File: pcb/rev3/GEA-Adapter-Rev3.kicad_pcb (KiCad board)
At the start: 2 copper layers, 88.7 x 40 mm, 109 parts, among them J1 8P8C, J3 TC2030, J4 USB_C_Receptacle_USB2.0_16P, Q3 CJ3407, Q4 CJ3407, Q5 MMBT3904, SW1 SW_Push, SW2 SW_Push, U10 TPS22810DBVR, U2 ESP32-C3-WROOM-02, U4 74LVC2G07, U5 74LVC2G07_3v3, U6 AP2112K-3.3, U7 USBLC6-2SC6, U8 AP63205WU, U9 TPS22810DBVR

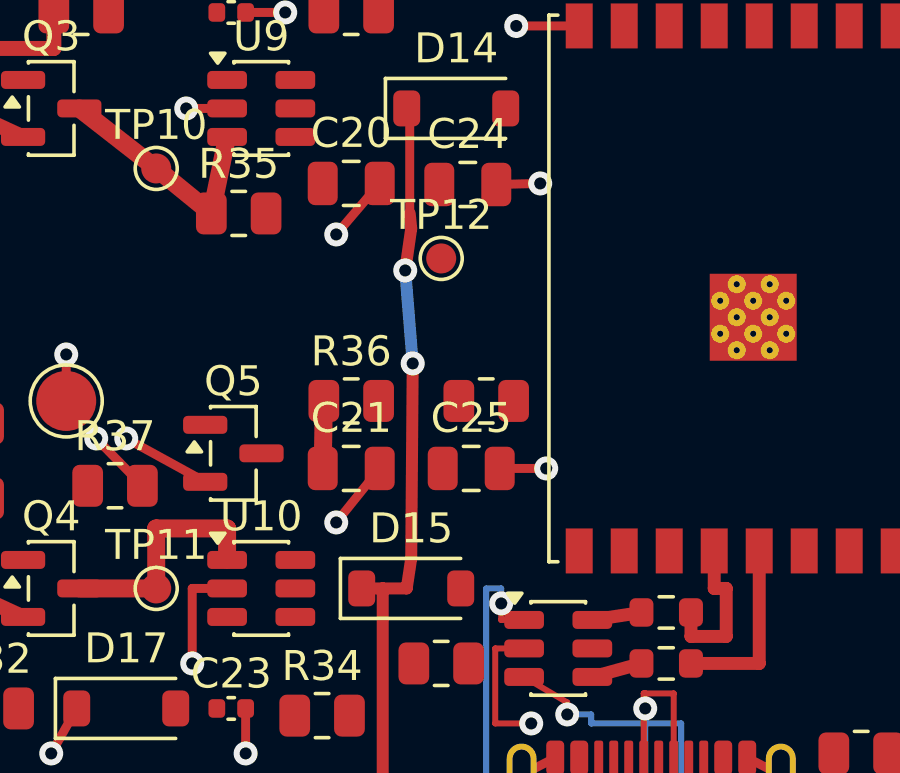
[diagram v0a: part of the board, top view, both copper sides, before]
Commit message: feat(pcb): route rev3a switch outputs
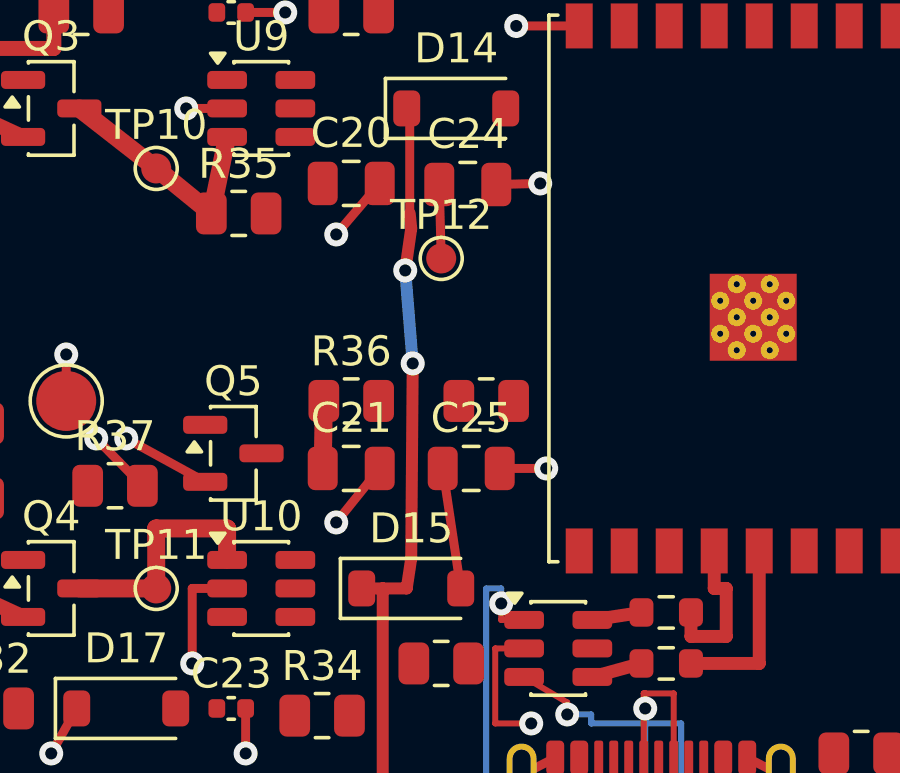
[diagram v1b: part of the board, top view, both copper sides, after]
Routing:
- net PIN3_SW_OUT: track 0.00 -> 4.04 mm
- net PIN1_SW_OUT: track 0.00 -> 2.47 mm
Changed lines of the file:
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@@
+	)
+	(segment
+		(start 65.05 23)
+		(end 65.65 27)
+		(width 0.3)
+		(layer "F.Cu")
+		(net 44)
 	)
 	(segment
@@
 	)
 	(segment
+		(start 64.935456 13.535277)
+		(end 65 16)
+		(width 0.3)
+		(layer "F.Cu")
+		(net 47)
+	)
+	(segment

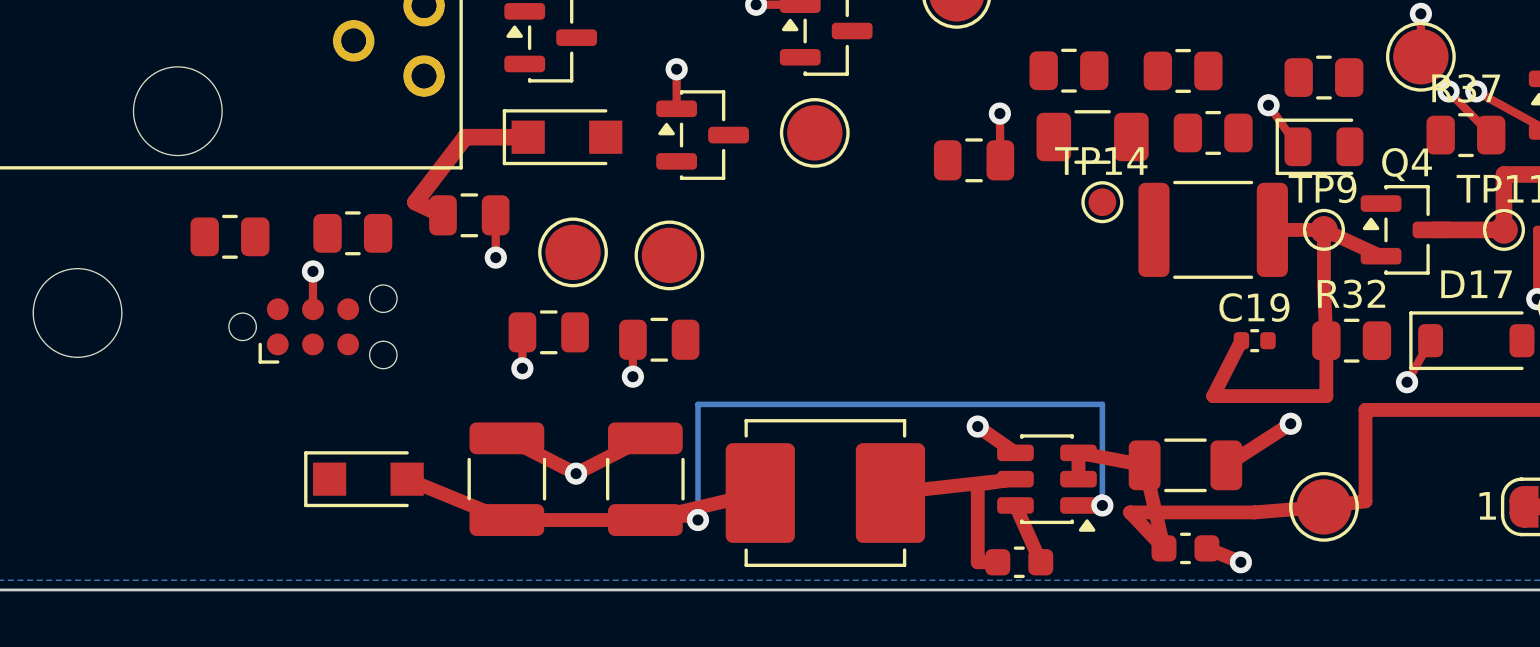
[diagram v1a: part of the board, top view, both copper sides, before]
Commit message: feat(pcb): reinforce rev3a buck output path
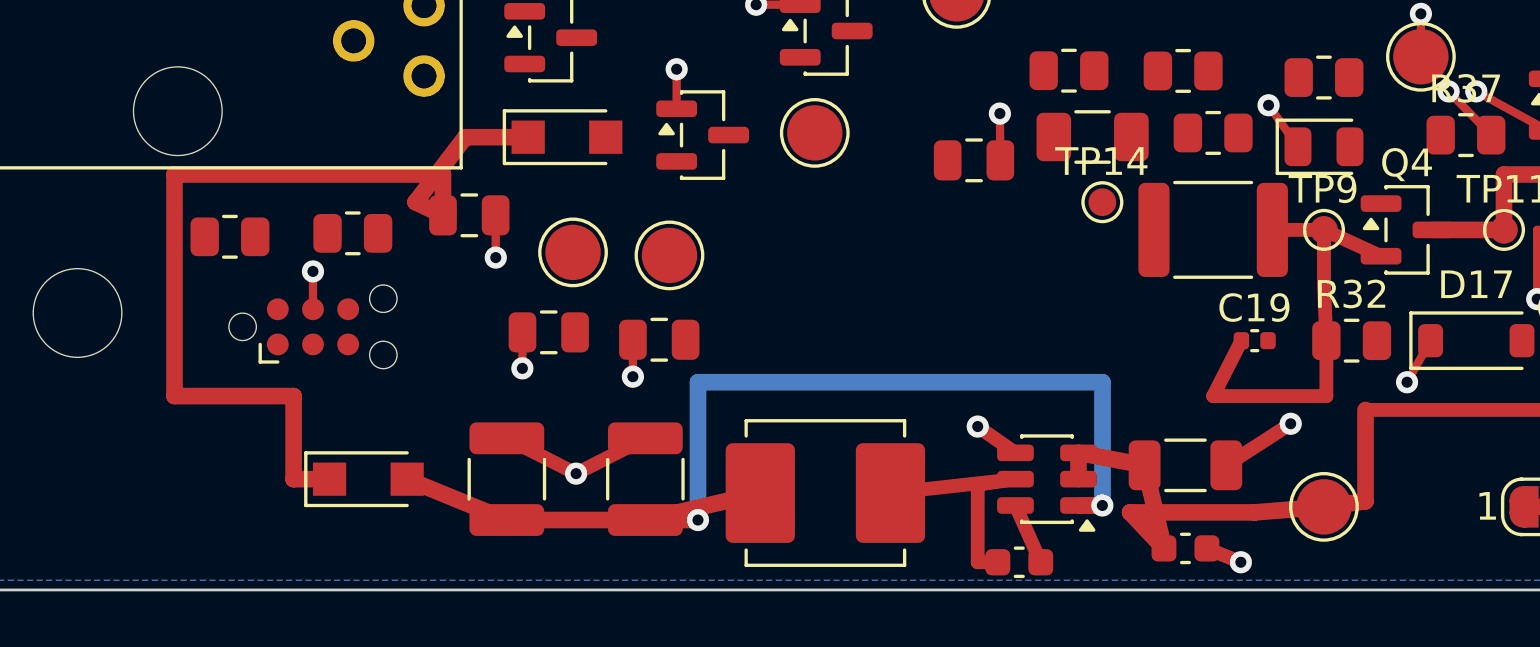
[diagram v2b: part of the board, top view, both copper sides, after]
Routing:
- net +5V: track 6.33 -> 34.1 mm
- net /BUCK_5V: track 38.3 -> 39.9 mm
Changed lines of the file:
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@@
+	)
+	(segment
+		(start 17.1947 25)
+		(end 17.1947 26.4745)
+		(width 0.6)
+		(layer "F.Cu")
+		(net 2)
 	)
 	(segment
@@
 	)
 	(segment
+		(start 7.5 33)
+		(end 7.5 25)
+		(width 0.6)
+		(layer "F.Cu")
+		(net 2)
+	)
+	(segment
+		(start 11.8 33)
+		(end 7.5 33)
+		(width 0.6)
+		(layer "F.Cu")
+		(net 2)
+	)
+	(segment
+		(start 13.1 36)
+		(end 11.8 36)
+		(width 0.6)
+		(layer "F.Cu")
+		(net 2)
+	)
+	(segment
+		(start 7.5 25)
+		(end 17.1947 25)
+		(width 0.6)
+		(layer "F.Cu")
+		(net 2)
+	)
+	(segment
 		(start 18 23.653262)
 		(end 16.2 26)
@@
 	)
 	(segment
+		(start 11.8 36)
+		(end 11.8 33)
+		(width 0.6)
+		(layer "F.Cu")
+		(net 2)
+	)
+	(segment
 		(start 16.2 26)
 		(end 17.194716 26.474524)
@@
 		(start 19.5 37.475)
 		(end 15.9 36)
-		(width 0.5)
+		(width 0.6)
 		(layer "F.Cu")
 		(net 5)
@@
 		(start 26.4 37.475)
 		(end 24.5 37.475)
-		(width 0.2)
+		(width 0.6)
 		(layer "F.Cu")
 		(net 5)
@@
 		(start 28.65 36.5)
 		(end 24.5 37.475)
-		(width 0.5)
+		(width 0.6)
 		(layer "F.Cu")
 		(net 5)
@@
 		(start 24.5 37.475)
 		(end 19.5 37.475)
-		(width 0.5)
+		(width 0.6)
 		(layer "F.Cu")
 		(net 5)
@@
 		(start 40.1375 36.95)
 		(end 41 36.95)
-		(width 0.2)
+		(width 0.6)
 		(layer "F.Cu")
 		(net 5)
@@
 	)
 	(segment
-		(start 41 33.299999)
-		(end 26.4 33.299999)
-		(width 0.2)
+		(start 41 32.5)
+		(end 26.4 32.5)
+		(width 0.6)
 		(layer "B.Cu")
 		(net 5)
 	)
 	(segment
-		(start 26.4 33.299999)
+		(start 26.4 32.5)
 		(end 26.4 37.475)
-		(width 0.2)
+		(width 0.6)
 		(layer "B.Cu")
 		(net 5)
@@
 	(segment
 		(start 41 36.95)
-		(end 41 33.299999)
-		(width 0.2)
+		(end 41 32.5)
+		(width 0.6)
 		(layer "B.Cu")
 		(net 5)
@@
 		(start 50.5 36.8)
 		(end 49 37)
-		(width 0.5)
+		(width 0.6)
 		(layer "F.Cu")
 		(net 61)
@@
 		(start 40.1375 36)
 		(end 40.1375 35.05)
-		(width 0.5)
+		(width 0.6)
 		(layer "F.Cu")
 		(net 61)
@@
 		(start 42.525 35.5)
 		(end 43.225 38.5)
-		(width 0.5)
+		(width 0.6)
 		(layer "F.Cu")
 		(net 61)
@@
 		(start 40.1375 35.05)
 		(end 42.525 35.5)
-		(width 0.5)
+		(width 0.6)
 		(layer "F.Cu")
 		(net 61)
@@
 		(start 42 37.2)
 		(end 46.5 37.2)
-		(width 0.5)
+		(width 0.6)
 		(layer "F.Cu")
 		(net 61)
@@
 		(start 46.5 37.2)
 		(end 49 37)
-		(width 0.5)
+		(width 0.6)
 		(layer "F.Cu")
 		(net 61)
@@
 		(start 43.225 38.5)
 		(end 42 37.2)
-		(width 0.5)
+		(width 0.6)
 		(layer "F.Cu")
 		(net 61)
@@
 		(start 50.5 33.5)
 		(end 50.5 36.8)
-		(width 0.5)
-		(layer "F.Cu")
-		(net 61)
+		(width 0.6)
+		(layer "F.Cu")
+		(net 61)

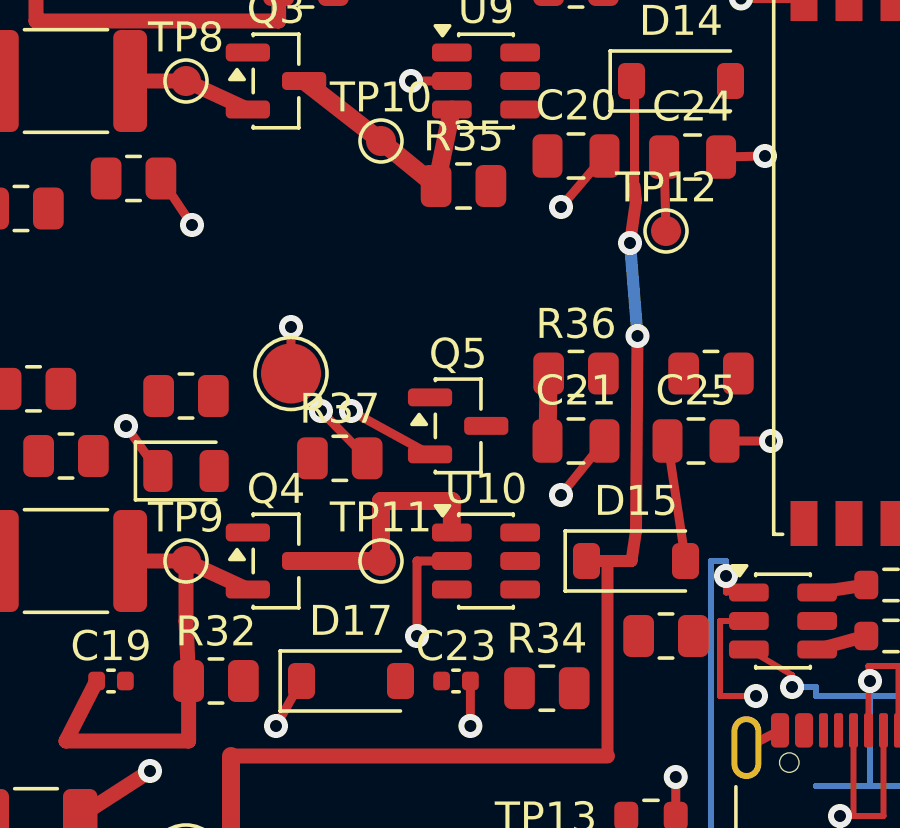
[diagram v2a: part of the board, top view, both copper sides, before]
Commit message: feat(pcb): route rev3a input priority controls
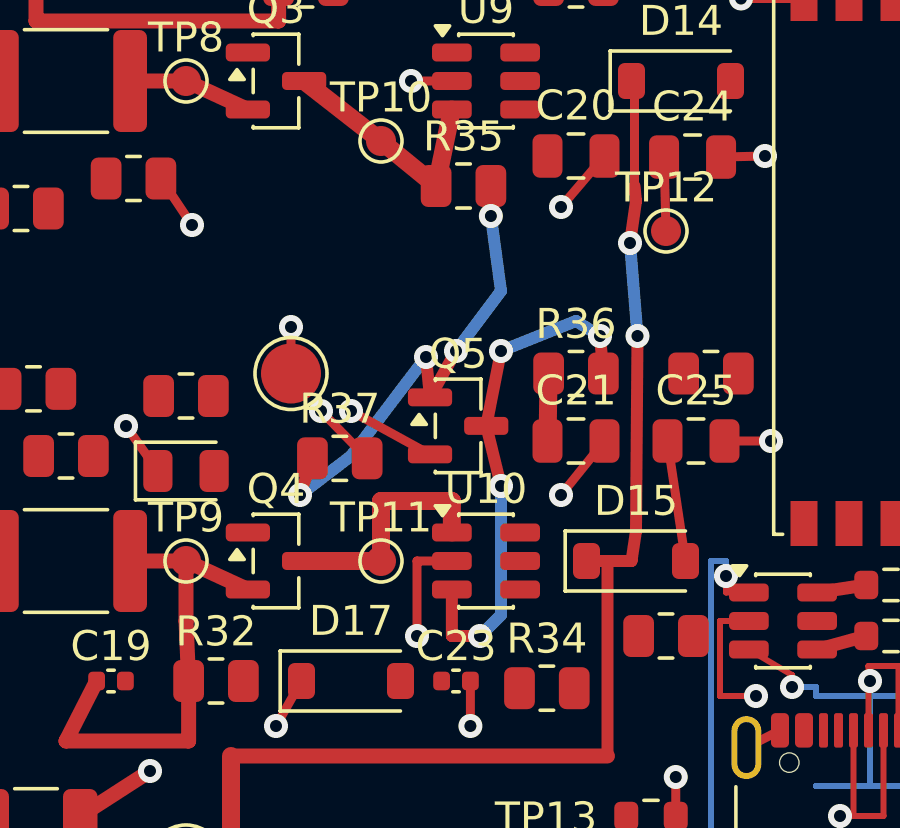
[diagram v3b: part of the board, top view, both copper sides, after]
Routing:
- net PIN3_EN: track 0.00 -> 17.3 mm, vias 0 -> 4
- net PRIORITY_BASE: track 0.00 -> 16.7 mm, vias 0 -> 4
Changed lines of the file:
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@@
+	)
+	(segment
+		(start 58.8 29.5)
+		(end 57.8625 29.5)
+		(width 0.4)
+		(layer "F.Cu")
+		(net 57)
+	)
+	(segment
+		(start 59.00875 22.496204)
+		(end 59.5 24.5)
+		(width 0.4)
+		(layer "F.Cu")
+		(net 57)
+	)
+	(segment
+		(start 59.00875 22.496204)
+		(end 59.5 20)
+		(width 0.4)
+		(layer "F.Cu")
+		(net 57)
+	)
+	(segment
+		(start 57.8625 29.5)
+		(end 57.8625 27.95)
+		(width 0.4)
+		(layer "F.Cu")
+		(net 57)
+	)
+	(segment
+		(start 62.8 19.5)
+		(end 62.9125 20.75)
+		(width 0.4)
+		(layer "F.Cu")
+		(net 57)
+	)
+	(via
+		(at 59.5 24.5)
+		(size 0.8)
+		(drill 0.4)
+		(layers "F.Cu" "B.Cu")
+		(net 57)
+	)
+	(via
+		(at 62.8 19.5)
+		(size 0.8)
+		(drill 0.4)
+		(layers "F.Cu" "B.Cu")
+		(net 57)
+	)
+	(via
+		(at 59.5 20)
+		(size 0.8)
+		(drill 0.4)
+		(layers "F.Cu" "B.Cu")
+		(net 57)
+	)
+	(via
+		(at 58.8 29.5)
+		(size 0.8)
+		(drill 0.4)
+		(layers "F.Cu" "B.Cu")
+		(net 57)
+	)
+	(segment
+		(start 59.5 20)
+		(end 62 19)
+		(width 0.4)
+		(layer "B.Cu")
+		(net 57)
+	)
+	(segment
+		(start 59.5 28.8)
+		(end 58.8 29.5)
+		(width 0.4)
+		(layer "B.Cu")
+		(net 57)
+	)
+	(segment
+		(start 59.5 24.5)
+		(end 59.5 28.8)
+		(width 0.4)
+		(layer "B.Cu")
+		(net 57)
+	)
+	(segment
+		(start 62 19)
+		(end 62.8 19.5)
+		(width 0.4)
+		(layer "B.Cu")
+		(net 57)
 	)
 	(segment
@@
 	)
 	(segment
+		(start 53.214739 23.577704)
+		(end 52.8 24.8)
+		(width 0.4)
+		(layer "F.Cu")
+		(net 60)
+	)
+	(segment
+		(start 57.13375 21.546204)
+		(end 58 20)
+		(width 0.4)
+		(layer "F.Cu")
+		(net 60)
+	)
+	(segment
+		(start 57 20.2)
+		(end 57.13375 21.546204)
+		(width 0.4)
+		(layer "F.Cu")
+		(net 60)
+	)
+	(segment
+		(start 59.1625 15.5)
+		(end 59.1625 14.5)
+		(width 0.4)
+		(layer "F.Cu")
+		(net 60)
+	)
+	(via
+		(at 59.1625 15.5)
+		(size 0.8)
+		(drill 0.4)
+		(layers "F.Cu" "B.Cu")
+		(net 60)
+	)
+	(via
+		(at 57 20.2)
+		(size 0.8)
+		(drill 0.4)
+		(layers "F.Cu" "B.Cu")
+		(net 60)
+	)
+	(via
+		(at 58 20)
+		(size 0.8)
+		(drill 0.4)
+		(layers "F.Cu" "B.Cu")
+		(net 60)
+	)
+	(via
+		(at 52.8 24.8)
+		(size 0.8)
+		(drill 0.4)
+		(layers "F.Cu" "B.Cu")
+		(net 60)
+	)
+	(segment
+		(start 59.5 18)
+		(end 59.1625 15.5)
+		(width 0.4)
+		(layer "B.Cu")
+		(net 60)
+	)
+	(segment
+		(start 54.5 23.5)
+		(end 57 20.2)
+		(width 0.4)
+		(layer "B.Cu")
+		(net 60)
+	)
+	(segment
+		(start 58 20)
+		(end 59.5 18)
+		(width 0.4)
+		(layer "B.Cu")
+		(net 60)
+	)
+	(segment
+		(start 52.8 24.8)
+		(end 54.5 23.5)
+		(width 0.4)
+		(layer "B.Cu")
+		(net 60)
+	)
+	(segment

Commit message: fix(pcb): place rev3a antenna beyond board edge
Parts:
- moved U2 6.00 mm to (81.6, 17.0)
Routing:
- net USB_MCU_P: track 6.02 -> 12.0 mm
- net USB_MCU_N: track 5.23 -> 11.2 mm
- net GND: track 97.9 -> 103.9 mm
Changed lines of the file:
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@@
 	(footprint "RF_Module:ESP32-C3-WROOM-02"
 		(layer "F.Cu")
-		(at 75.6 17 -90)
+		(at 81.6 17 -90)
 		(descr "RF Module, ESP32-C3 WROOM-02, Wi-Fi and Bluetooth, BLE, onboard antenna, https://www.espressif.com/sites/default/files/documentation/esp32-c3-wroom-02_datasheet_en.pdf")
 		(tags "ESP32-C3 WROOM-02 espressif")
@@
 			(polygon
 				(pts
-					(xy 82.7 3) (xy 82.7 31) (xy 93.7 31) (xy 93.7 3)
+					(xy 88.7 3) (xy 88.7 31) (xy 99.7 31) (xy 99.7 3)
 				)
 			)
@@
 	)
 	(segment
-		(start 69.6 8.25)
-		(end 67.5 8.25)
-		(width 0.3)
-		(layer "F.Cu")
-		(net 18)
-	)
-	(segment
 		(start 19.5 34.525)
 		(end 22 35.8)
@@
 	)
 	(segment
+		(start 75.6 8.25)
+		(end 67.5 8.25)
+		(width 0.3)
+		(layer "F.Cu")
+		(net 18)
+	)
+	(segment
 		(start 48.0625 24)
 		(end 47 22.5)
@@
 	)
 	(segment
-		(start 75.6 25.75)
+		(start 81.6 28)
+		(end 75.6 28)
+		(width 0.432)
+		(layer "F.Cu")
+		(net 63)
+	)
+	(segment
+		(start 75.6 28)
 		(end 75.6 29.5)
 		(width 0.432)
@@
 	)
 	(segment
+		(start 81.6 25.75)
+		(end 81.6 28)
+		(width 0.432)
+		(layer "F.Cu")
+		(net 63)
+	)
+	(segment
 		(start 74.5 28.6)
 		(end 73.325 28.6)
@@
 	)
 	(segment
+		(start 80.1 25.75)
+		(end 80.1 27)
+		(width 0.432)
+		(layer "F.Cu")
+		(net 64)
+	)
+	(segment
 		(start 73.325 28.6)
 		(end 73.325 27.8)
@@
 	)
 	(segment
-		(start 74.1 25.75)
+		(start 80.1 27)
 		(end 74.1 27)
 		(width 0.432)

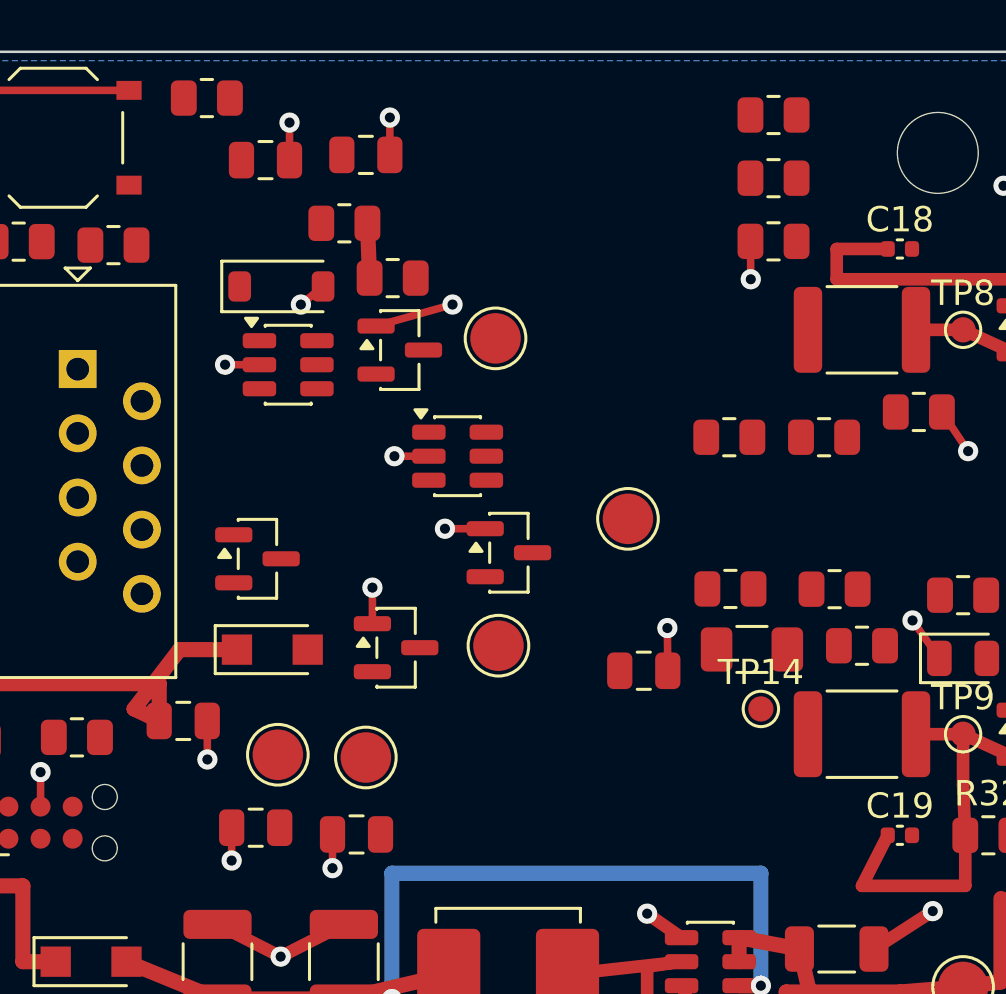
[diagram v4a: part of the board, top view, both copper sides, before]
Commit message: feat(pcb): route rev3a 5v distribution
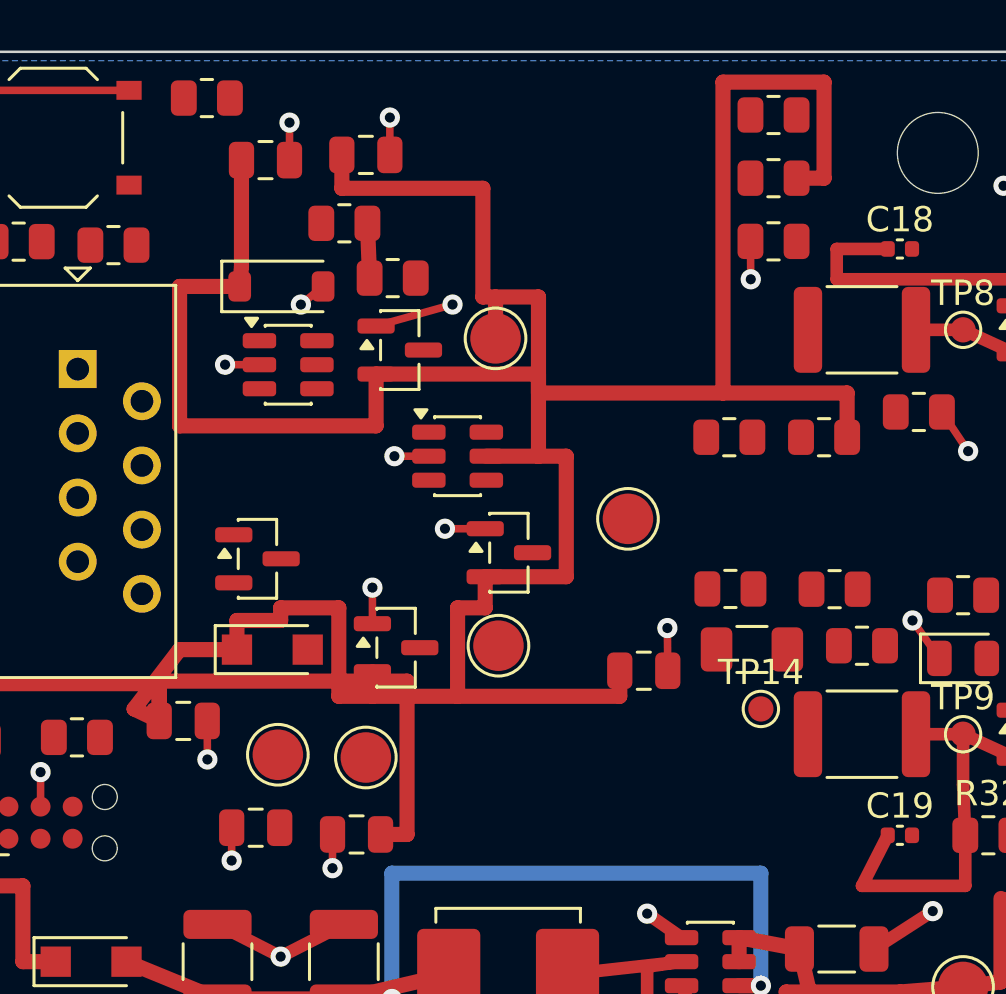
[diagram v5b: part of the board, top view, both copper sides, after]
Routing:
- net +5V: track 34.1 -> 178.2 mm
